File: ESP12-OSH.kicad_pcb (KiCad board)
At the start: 2 copper layers, 46.1 x 38.2 mm, 23 parts, among them P1 CONN_01X02, P2 CONN_01X06, P3 CONN_01X08, P4 CONN_01X08, SW1 SW_Push, SW2 SW_Push, U1 ESP-12E

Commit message: version 2 in the works!
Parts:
- removed REF***: OSHW-Logo_5.7x6mm_SilkScreen, Symbols:OSHW-Logo_5.7x6mm_SilkScreen
- added LOGO: , ESP12:newlogo, F.Cu at (168.3, 104.1)
- H1: footprint TO_SOT_Packages_THT:TO-92_Inline_Narrow_Oval -> TO_SOT_Packages_THT:TO-92_Inline_Wide
- moved SW1 65.0 mm to (138.9, 131.4)
- moved SW2 64.4 mm to (179.1, 131.4), turned to 180 degrees
- moved P1 34.6 mm to (178.7, 97.5)
- moved D1 33.5 mm to (166.2, 93.7), turned to 180 degrees
- moved C1 33.5 mm to (146.2, 122.4), turned to 270 degrees
- moved H1 32.1 mm to (174.0, 96.8), turned to 270 degrees
- moved R1 31.8 mm to (141.1, 105.0)
- moved JP2 31.4 mm to (132.8, 99.9)
- moved JP1 31.4 mm to (150.6, 94.1), turned to 270 degrees
- moved R7 30.7 mm to (144.5, 90.9), turned to 180 degrees
- moved P3 29.0 mm to (132.8, 121.4)
- moved R2 29.0 mm to (144.5, 110.4)
- moved R3 28.8 mm to (153.7, 94.4), turned to 0 degrees
- moved R4 27.8 mm to (166.5, 120.8)
- moved U1 27.8 mm to (148.5, 105.0)
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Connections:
- H1 pad 1: /VIN -> GND
- H1 pad 2: GND -> /VIN
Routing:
- net /REST: track 21.7 -> 64.3 mm
- net /ADC: track 11.9 -> 51.9 mm
- net Net-(JP3-Pad1): track 0.00 -> 12.2 mm
- net /GPIO0: track 33.7 -> 43.0 mm
- net GND: track 6.23 -> 0.00 mm
- net Net-(JP1-Pad1): track 9.33 -> 3.15 mm
- net /GPIO13: track 11.8 -> 16.8 mm
- net /GPIO14: track 11.4 -> 16.0 mm
- net /GPIO12: track 11.6 -> 16.2 mm
- net /VIN: track 7.33 -> 11.5 mm, vias 1 -> 0
- net /TX: track 15.5 -> 16.7 mm
- net /MOSI: track 3.68 -> 4.86 mm
- net /VCC: track 121.2 -> 122.3 mm
- net Net-(D1-Pad2): track 3.77 -> 2.68 mm
- net /RX: track 15.7 -> 16.4 mm
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- added copper zone on B.Cu, net GND
- removed copper zone on B.Cu, net /GND
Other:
- board size 46.1 x 38.2 mm -> 51.2 x 44.2 mm
- board text added: "ESP Board v2"
- board text added: "LED"
- board text added: "V-divider"
- board text added: "flash"
- board text added: "reset"
- board text added: "sleep"
- board text removed: "ESP Board v2.0 2017"

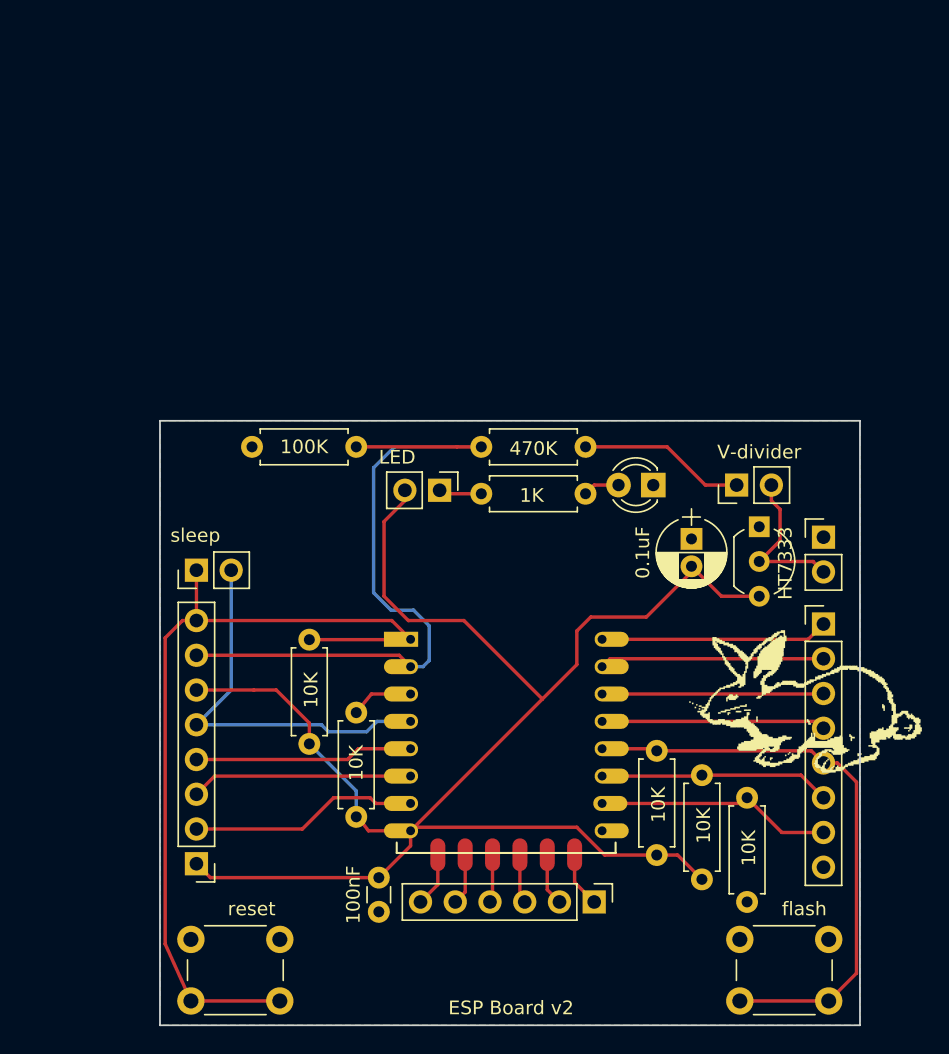
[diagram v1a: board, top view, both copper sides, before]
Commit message: thicker traces, antenna outside of pcb, shorter traces, removed custom HT7333 footprint
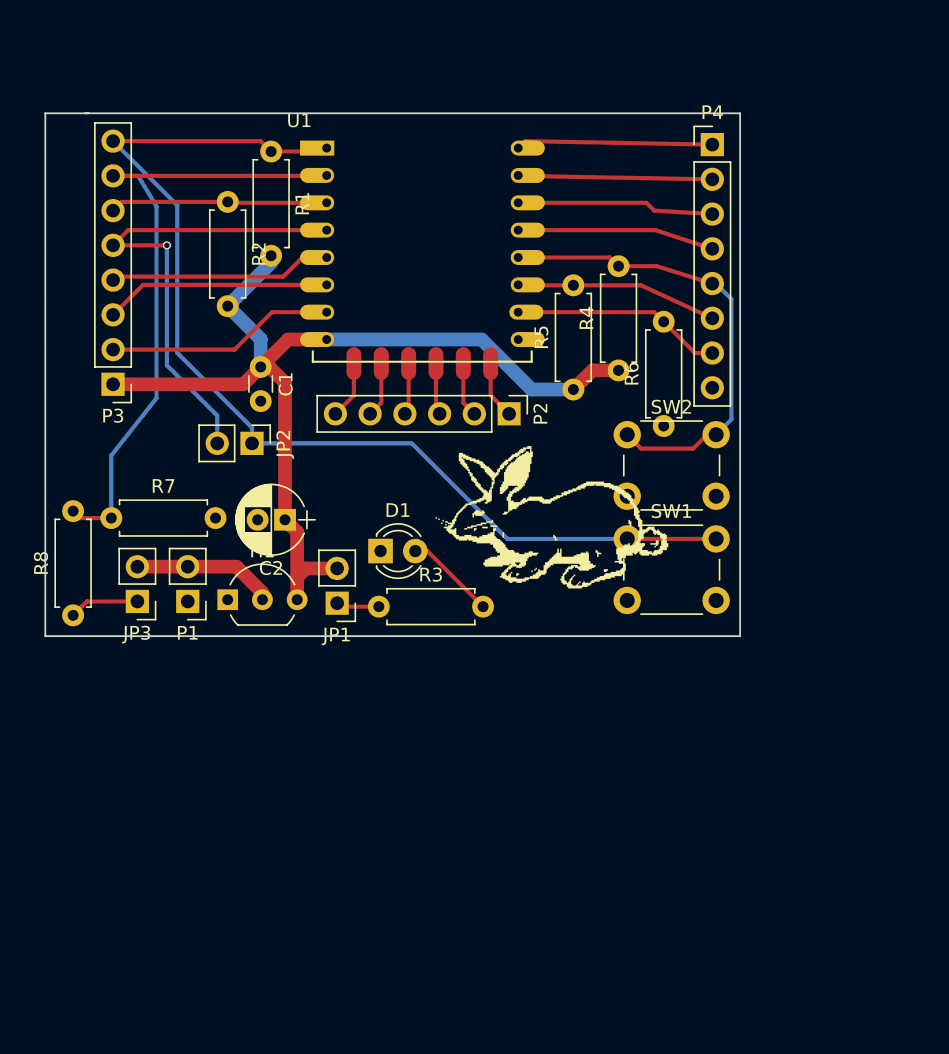
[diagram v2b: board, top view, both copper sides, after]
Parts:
- moved P1 46.7 mm to (132.2, 102.2), turned to 180 degrees
- moved JP3 44.6 mm to (128.5, 102.2), turned to 180 degrees
- moved SW2 43.9 mm to (164.3, 90.0), turned to 0 degrees
- moved SW1 42.3 mm to (164.3, 97.7), turned to 0 degrees
- moved R8 39.4 mm to (123.8, 103.3), turned to 90 degrees
- moved H1 39.2 mm to (135.1, 102.1), turned to 0 degrees
- moved R2 38.5 mm to (135.1, 73.0)
- moved C1 38.3 mm to (137.5, 85.1)
- moved R5 37.0 mm to (160.4, 86.7)
- moved U1 36.4 mm to (142.4, 69.1)
- moved P2 36.2 mm to (155.7, 88.5)
- moved P4 36.0 mm to (170.6, 68.8)
- moved R1 35.8 mm to (138.3, 69.3)
- moved P3 35.6 mm to (126.7, 86.4)
- moved R4 35.5 mm to (163.7, 85.3)
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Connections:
- C2 pad 1: GND -> /VCC
- C2 pad 2: /VCC -> GND
- P3 pad 6: /VCC -> /CH_PD
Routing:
- net /VCC: track 122.3 -> 73.0 mm
- net /REST: track 64.3 -> 79.2 mm
- net /CH_PD: track 4.62 -> 15.9 mm
- net /GPIO0: track 43.0 -> 34.4 mm
- net /GPIO16: track 28.5 -> 36.0 mm, vias 0 -> 1
- net Net-(JP3-Pad1): track 12.2 -> 5.12 mm
- net /ADC: track 51.9 -> 47.5 mm
- net Net-(D1-Pad2): track 2.68 -> 6.64 mm
- net /TX: track 16.7 -> 14.4 mm
- net /RX: track 16.4 -> 14.2 mm
- net /GPIO2: track 16.9 -> 14.7 mm
- net /GPIO4: track 16.4 -> 14.4 mm
- net /GPIO15: track 17.4 -> 15.4 mm
- net /GPIO5: track 16.2 -> 14.4 mm
- net /VIN: track 11.5 -> 10.4 mm
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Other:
- board size 51.2 x 44.2 mm -> 50.8 x 38.2 mm
- net class Default: trace_width 0.25 -> 0.3
- net class POWER added: clearance 0.2, trace_width 1, via_dia 0.6, via_drill 0.4
- rule trace_min: 0.2 -> 0.3
- board text removed: "ESP Board v2"
- board text removed: "LED"
- board text removed: "V-divider"
- board text removed: "flash"
- board text removed: "reset"
- board text removed: "sleep"

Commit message: text on back and front silk improved
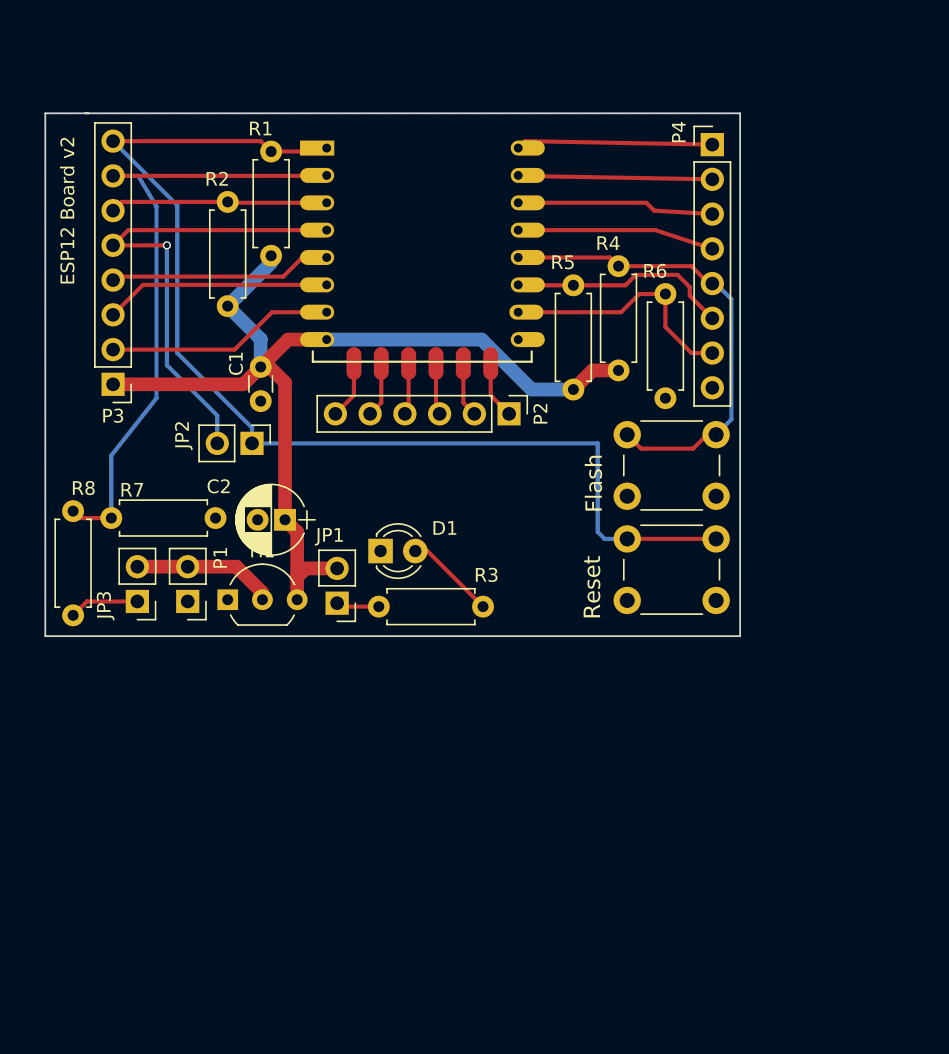
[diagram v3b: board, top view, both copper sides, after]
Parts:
- LOGO: moved to B.Cu
- moved LOGO 15.7 mm to (155.2, 75.9), turned to 180 degrees
- moved R6 2.04 mm to (167.1, 87.4)
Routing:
- net /REST: track 79.2 -> 83.0 mm
- net /GPIO15: track 15.4 -> 17.9 mm
- net /GPIO2: track 14.7 -> 16.2 mm
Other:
- board text added: "0"
- board text added: "12"
- board text added: "13"
- board text added: "14"
- board text added: "15"
- board text added: "16"
- board text added: "2"
- board text added: "4"
- board text added: "5"
- board text added: "ADC"
- board text added: "CH_PD"
- board text added: "CLK"
- board text added: "CS0"
- board text added: "ESP12 Board v2"
- board text added: "Flash"
- board text added: "GND"
- board text added: "MISO"
- board text added: "MOSI"
- board text added: "REST"
- board text added: "RX"
- board text added: "Reset"
- board text added: "SPIHD"
- board text added: "SPIWP"
- board text added: "TX"
- board text added: "VCC"

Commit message: mini tweaks before sending the design to the manufacturer
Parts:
- renumbered JP3 to ADC, P1 to IN, JP1 to LED, JP2 to SLEEP
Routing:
- net /ADC: track 47.5 -> 46.7 mm
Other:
- outline, holes or cut-outs redrawn
- board text added: "+"
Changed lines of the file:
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@@
     (links 59)
     (no_connects 0)
-    (area 121.729499 66.484499 172.656501 104.838501)
+    (area 121.729499 60.112999 178.114002 108.239501)
     (thickness 1.6)
-    (drawings 30)
+    (drawings 32)
     (tracks 124)
     (zones 0)
@@
   (page A4)
   (layers
-    (0 F.Cu signal)
+    (0 F.Cu signal hide)
     (31 B.Cu signal)
     (32 B.Adhes user)
@@
     (visible_elements FFFFFF7F)
     (pcbplotparams
-      (layerselection 0x00030_80000001)
+      (layerselection 0x3ffff_80000001)
       (usegerberextensions false)
       (excludeedgelayer true)
@@
       (outputformat 1)
       (mirror false)
-      (drillshape 1)
+      (drillshape 0)
       (scaleselection 1)
-      (outputdirectory ""))
+      (outputdirectory "../../../../../../home/thijs/Documents/KiCad/ESP12 Export/"))
   )
   (net 0 "")
@@
     (descr "Through hole straight pin header, 1x02, 2.54mm pitch, single row")
     (tags "Through hole pin header THT 1x02 2.54mm single row")
-    (fp_text reference JP1 (at 0.508 4.953 180) (layer F.SilkS)
+    (fp_text reference LED (at 0 4.953 180) (layer F.SilkS)
       (effects (font (size 1 1) (thickness 0.15)))
     )
@@
     (descr "Through hole straight pin header, 1x02, 2.54mm pitch, single row")
     (tags "Through hole pin header THT 1x02 2.54mm single row")
-    (fp_text reference JP2 (at -0.635 5.08 270) (layer F.SilkS)
+    (fp_text reference SLEEP (at -0.635 5.08 270) (layer F.SilkS)
       (effects (font (size 1 1) (thickness 0.15)))
     )
@@
     (descr "Through hole straight pin header, 1x02, 2.54mm pitch, single row")
     (tags "Through hole pin header THT 1x02 2.54mm single row")
-    (fp_text reference JP3 (at 2.413 -0.254 270) (layer F.SilkS)
+    (fp_text reference ADC (at 2.413 -0.254 270) (layer F.SilkS)
       (effects (font (size 1 1) (thickness 0.15)))
     )
@@
     (descr "Through hole straight pin header, 1x02, 2.54mm pitch, single row")
     (tags "Through hole pin header THT 1x02 2.54mm single row")
-    (fp_text reference P1 (at -2.413 3.175 450) (layer F.SilkS)
+    (fp_text reference IN (at -2.413 3.175 270) (layer F.SilkS) hide
       (effects (font (size 1 1) (thickness 0.15)))
     )
@@
       (effects (font (size 1 1) (thickness 0.15)))
     )
-    (fp_text value CONN_01X08 (at 0 20.11 180) (layer F.Fab)
+    (fp_text value CONN_01X08 (at -0.508 18.669 180) (layer F.Fab)
       (effects (font (size 1 1) (thickness 0.15)))
     )
@@
       (xy 11.2 -10.5)) (layer B.SilkS) (width 0.01))
   )
+  (gr_text + (at 132.207 98.044) (layer F.SilkS)
+    (effects (font (size 0.6 0.6) (thickness 0.127)))
+  )
+  (dimension 50.8 (width 0.127) (layer Eco1.User)
+    (gr_text "50,800 mm" (at 147.193 107.696) (layer Eco1.User)
+      (effects (font (size 0.6 0.6) (thickness 0.127)))
+    )
+    (feature1 (pts (xy 172.593 107.696) (xy 172.593 107.696)))
+    (feature2 (pts (xy 121.793 107.696) (xy 121.793 107.696)))
+    (crossbar (pts (xy 121.793 107.696) (xy 172.593 107.696)))
+    (arrow1a (pts (xy 172.593 107.696) (xy 171.466496 108.282421)))
+    (arrow1b (pts (xy 172.593 107.696) (xy 171.466496 107.109579)))
+    (arrow2a (pts (xy 121.793 107.696) (xy 122.919504 108.282421)))
+    (arrow2b (pts (xy 121.793 107.696) (xy 122.919504 107.109579)))
+  )
+  (dimension 38.227 (width 0.127) (layer Eco1.User)
+    (gr_text "38,227 mm" (at 175.514 85.6615 270) (layer Eco1.User)
+      (effects (font (size 0.6 0.6) (thickness 0.127)))
+    )
+    (feature1 (pts (xy 175.514 104.775) (xy 175.514 104.775)))
+    (feature2 (pts (xy 175.514 66.548) (xy 175.514 66.548)))
+    (crossbar (pts (xy 175.514 66.548) (xy 175.514 104.775)))
+    (arrow1a (pts (xy 175.514 104.775) (xy 174.927579 103.648496)))
+    (arrow1b (pts (xy 175.514 104.775) (xy 176.100421 103.648496)))
+    (arrow2a (pts (xy 175.514 66.548) (xy 174.927579 67.674504)))
+    (arrow2b (pts (xy 175.514 66.548) (xy 176.100421 67.674504)))
+  )
+  (gr_line (start 121.793 66.548) (end 172.593 66.548) (angle 90) (layer Edge.Cuts) (width 0.127))
+  (gr_line (start 121.793 104.775) (end 121.793 66.548) (angle 90) (layer Edge.Cuts) (width 0.127))
+  (gr_line (start 172.593 104.775) (end 121.793 104.775) (angle 90) (layer Edge.Cuts) (width 0.127))
+  (gr_line (start 172.593 66.548) (end 172.593 104.775) (angle 90) (layer Edge.Cuts) (width 0.127))
   (gr_text Flash (at 161.925 93.599 90) (layer F.SilkS)
     (effects (font (size 1.2 1.2) (thickness 0.2)))
@@
     (effects (font (size 1 1) (thickness 0.127)))
   )
-  (gr_line (start 121.793 66.548) (end 124.968 66.548) (angle 90) (layer Edge.Cuts) (width 0.127))
-  (gr_line (start 121.793 104.775) (end 121.793 66.548) (angle 90) (layer Edge.Cuts) (width 0.127))
-  (gr_line (start 172.593 104.775) (end 121.793 104.775) (angle 90) (layer Edge.Cuts) (width 0.127))
-  (gr_line (start 172.593 66.548) (end 172.593 104.775) (angle 90) (layer Edge.Cuts) (width 0.127))
-  (gr_line (start 124.714 66.548) (end 172.593 66.548) (angle 90) (layer Edge.Cuts) (width 0.127))
   (segment (start 163.703 85.344) (end 161.798 85.344) (width 1) (layer F.Cu) (net 1) (status 10))
   (segment (start 161.798 85.344) (end 160.401 86.741) (width 1) (layer F.Cu) (net 1))
@@
   (segment (start 146.177 102.616) (end 143.383 102.616) (width 0.3) (layer F.Cu) (net 5))
   (segment (start 143.383 102.616) (end 143.129 102.362) (width 0.3) (layer F.Cu) (net 5))
+  (segment (start 126.746 68.58) (end 127.508 68.58) (width 0.3) (layer B.Cu) (net 6))
+  (segment (start 127.508 68.58) (end 131.572 72.644) (width 0.3) (layer B.Cu) (net 6))
+  (segment (start 131.572 84.582) (end 136.906 89.916) (width 0.3) (layer B.Cu) (net 6))
+  (segment (start 131.572 72.644) (end 131.572 84.582) (width 0.3) (layer B.Cu) (net 6))
+  (segment (start 136.906 89.916) (end 136.906 90.678) (width 0.3) (layer B.Cu) (net 6))
   (segment (start 164.338 97.663) (end 162.687 97.663) (width 0.3) (layer B.Cu) (net 6))
   (segment (start 162.179 90.678) (end 136.906 90.678) (width 0.3) (layer B.Cu) (net 6))
@@
   (segment (start 162.687 97.663) (end 162.179 97.155) (width 0.3) (layer B.Cu) (net 6))
   (segment (start 164.338 97.663) (end 170.838 97.663) (width 0.3) (layer F.Cu) (net 6))
-  (segment (start 136.906 90.678) (end 136.906 89.535) (width 0.3) (layer B.Cu) (net 6))
-  (segment (start 131.445 73.279) (end 126.746 68.58) (width 0.3) (layer B.Cu) (net 6) (status 20))
-  (segment (start 131.445 84.074) (end 131.445 73.279) (width 0.3) (layer B.Cu) (net 6))
-  (segment (start 136.906 89.535) (end 131.445 84.074) (width 0.3) (layer B.Cu) (net 6))
   (segment (start 138.303 69.342) (end 142.113 69.342) (width 0.3) (layer F.Cu) (net 6))
   (segment (start 142.113 69.342) (end 142.367 69.088) (width 0.3) (layer F.Cu) (net 6))
@@
   (segment (start 139.192 78.486) (end 127 78.486) (width 0.3) (layer F.Cu) (net 17) (status 20))
   (segment (start 127 78.486) (end 126.746 78.74) (width 0.3) (layer F.Cu) (net 17) (status 30))
-  (segment (start 126.619 96.139) (end 126.619 91.567) (width 0.3) (layer B.Cu) (net 18))
-  (segment (start 128.57889 71.12) (end 126.746 71.12) (width 0.3) (layer B.Cu) (net 18) (status 20))
-  (segment (start 129.921 73.35111) (end 128.57889 71.12) (width 0.3) (layer B.Cu) (net 18))
-  (segment (start 129.921 87.376) (end 129.921 73.35111) (width 0.3) (layer B.Cu) (net 18))
-  (segment (start 126.619 91.567) (end 129.921 87.376) (width 0.3) (layer B.Cu) (net 18))
+  (segment (start 126.619 96.139) (end 126.619 93.599) (width 0.3) (layer B.Cu) (net 18))
+  (segment (start 129.794 74.168) (end 126.746 71.12) (width 0.3) (layer B.Cu) (net 18))
+  (segment (start 129.794 90.424) (end 129.794 74.168) (width 0.3) (layer B.Cu) (net 18))
+  (segment (start 126.619 93.599) (end 129.794 90.424) (width 0.3) (layer B.Cu) (net 18))
   (segment (start 126.619 96.139) (end 124.333 96.139) (width 0.3) (layer F.Cu) (net 18))
   (segment (start 124.333 96.139) (end 123.825 95.631) (width 0.3) (layer F.Cu) (net 18))
